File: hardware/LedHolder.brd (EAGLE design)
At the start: 8 x 8 mm, 5 parts

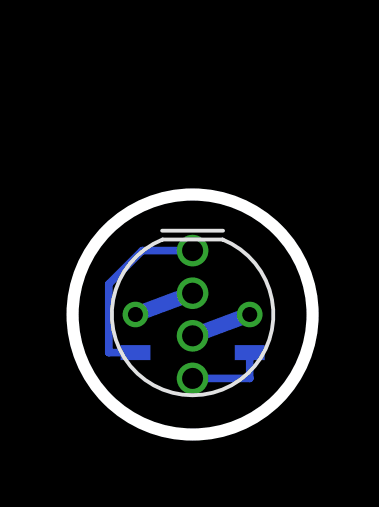
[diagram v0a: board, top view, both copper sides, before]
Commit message: More LedHolder updates
I switched the DataIn and DataOut connections to be through hole as
well since the holes hold the wire in place to make it easier for
soldering.
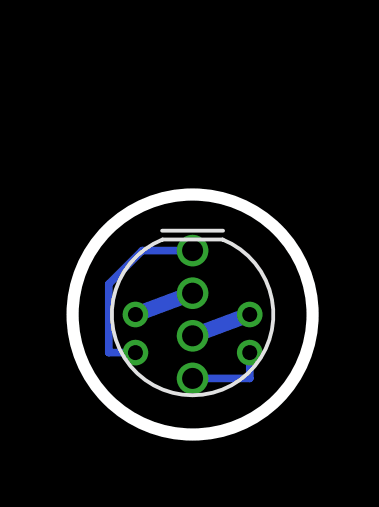
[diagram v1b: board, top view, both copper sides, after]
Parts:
- E$2, E$3: device adam_custom:PAD1MMX.5MM -> adam_custom:TP_5MM
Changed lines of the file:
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@@
 <element name="3" library="adam_custom" package="TP_5MM" value="" x="6.223" y="4.318"/>
 <element name="2" library="adam_custom" package="TP_5MM" value="" x="2.413" y="4.318"/>
-<element name="E$2" library="adam_custom" package="PAD1MMX.5MM" value="" x="6.223" y="3.048" rot="MR0"/>
-<element name="E$3" library="adam_custom" package="PAD1MMX.5MM" value="" x="2.413" y="3.048" rot="MR0"/>
+<element name="E$2" library="adam_custom" package="TP_5MM" value="" x="6.223" y="3.048" rot="MR0"/>
+<element name="E$3" library="adam_custom" package="TP_5MM" value="" x="2.413" y="3.048" rot="MR0"/>
 </elements>
 <signals>

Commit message: Create new LED holder PCB
The new PCB is rectangular and will extend horizontally from the end of
the branch wires. The LED will be bent at 90 degrees after being
soldered into this board so that it lays horizontally as well. I will
finalize the design once I have the flat cable in hand (currently on
order).
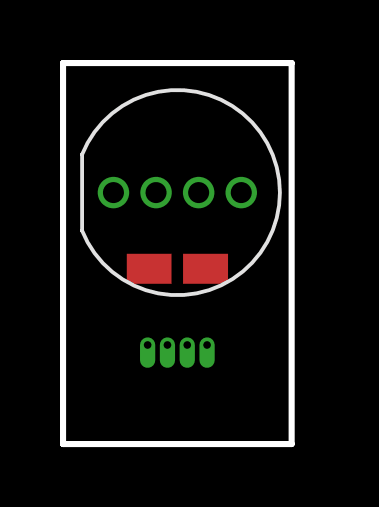
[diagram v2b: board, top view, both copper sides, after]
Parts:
- removed 2, 3: (no value), adam_custom:TP_5MM
- E$1: device adam_custom:LED-RGB-THRU -> adam_custom:NEOPIXEL_5MM_TH
- E$2: device adam_custom:TP_5MM -> adam_custom:NEOPIXEL_BRANCH_4WIRE
- E$3: value (none) -> 0.1uF; device adam_custom:TP_5MM -> adafruit:R0805W
- moved E$1 4.10 mm to (3.81, 8.38), turned to 180 degrees
- moved E$3 3.12 mm to (3.81, 5.84), flipped to the top
- moved E$2 2.43 mm to (3.81, 3.30), flipped to the top
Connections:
- net S$1: now also E$1.GROUND, E$2.P$1, E$3.1; no longer 2.P$1, E$1.2
- net S$2: now also E$1.5V, E$2.P$2, E$3.2; no longer 3.P$1, E$1.3
- net S$3: now also E$1.DATA_OUT, E$2.P$3; no longer E$1.1, E$3.P$1
- net S$4: now also E$1.DATA_IN, E$2.P$4; no longer E$1.4, E$2.P$1
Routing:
- net S$3: track 6.43 -> 0.00 mm
- net S$4: track 2.77 -> 0.00 mm
- net S$2: track 2.03 -> 0.00 mm
- net S$1: track 2.03 -> 0.00 mm
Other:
- board size 8 x 8 mm -> 7.6 x 12.7 mm
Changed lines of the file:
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@@
 <setting verticaltext="up"/>
 </settings>
-<grid distance="0.05" unitdist="inch" unit="inch" style="lines" multiple="1" display="yes" altdistance="0.01" altunitdist="inch" altunit="inch"/>
+<grid distance="0.05" unitdist="inch" unit="mil" style="lines" multiple="1" display="yes" altdistance="0.01" altunitdist="inch" altunit="mil"/>
 <layers>
 <layer number="1" name="Top" color="4" fill="1" visible="yes" active="yes"/>
@@
 <board>
 <plain>
-<circle x="4.318" y="4.318" radius="4" width="0.4064" layer="20"/>
-<text x="3.048" y="4.826" size="1.27" layer="22" font="vector" rot="MR0">-</text>
-<text x="6.604" y="4.826" size="1.27" layer="22" font="vector" rot="MR0">+</text>
-<text x="3.302" y="2.032" size="0.508" layer="22" font="vector" rot="MR0">Out</text>
-<text x="6.35" y="2.032" size="0.508" layer="22" font="vector" rot="MR0">In</text>
-<wire x1="3.302" y1="7.112" x2="5.334" y2="7.112" width="0.127" layer="21"/>
+<wire x1="0" y1="0" x2="0" y2="12.7" width="0.2032" layer="20"/>
+<wire x1="0" y1="12.7" x2="7.62" y2="12.7" width="0.2032" layer="20"/>
+<wire x1="7.62" y1="12.7" x2="7.62" y2="0" width="0.2032" layer="20"/>
+<wire x1="7.62" y1="0" x2="0" y2="0" width="0.2032" layer="20"/>
+<text x="5.588" y="0.508" size="1.016" layer="51" font="vector">In</text>
+<text x="0.508" y="0.508" size="1.016" layer="51" font="vector">Out</text>
+<text x="2.54" y="1.27" size="1.016" layer="51" font="vector">-</text>
+<text x="4.572" y="1.27" size="1.016" layer="51" font="vector">+</text>
 </plain>
 <attributes>
@@
 </class>
 </classes>
-<designrules name="LaenPCBOrder">
-<description language="de">&lt;b&gt;EAGLE Design Rules&lt;/b&gt;
+<designrules name="oshpark-2layer">
+<description language="en">&lt;b&gt;OSH Park Design Rules&lt;/b&gt;
 &lt;p&gt;
-Die Standard-Design-Rules sind so gewählt, dass sie für
-die meisten Anwendungen passen. Sollte ihre Platine
-besondere Anforderungen haben, treffen Sie die erforderlichen
-Einstellungen hier und speichern die Design Rules unter
-einem neuen Namen ab.</description>
-<description language="en">&lt;b&gt;Laen's PCB Order Design Rules&lt;/b&gt;
+Please make sure your boards conform to these design rules.
+&lt;/p&gt;
 &lt;p&gt;
-Please make sure your boards conform to these design rules.</description>
+Note, that not all DRC settings must be set by the manufacturer. Several can be adjusted for the design, including those listed on our docs page here.
+&lt;a href=&quot;http://docs.oshpark.com/design-tools/eagle/design-rules-files/&quot;&gt;Adjustable Settings&lt;/a&gt;
+&lt;/p&gt;</description>
 <param name="layerSetup" value="(1*16)"/>
-<param name="mtCopper" value="0.0356mm 0.0356mm 0.0356mm 0.0356mm 0.0356mm 0.0356mm 0.0356mm 0.0356mm 0.0356mm 0.0356mm 0.0356mm 0.0356mm 0.0356mm 0.0356mm 0.0356mm 0.0356mm"/>
-<param name="mtIsolate" value="1.5011mm 0.1499mm 0.2007mm 0.1499mm 0.2007mm 0.1499mm 0.2007mm 0.1499mm 0.2007mm 0.1499mm 0.2007mm 0.1499mm 0.2007mm 0.1499mm 0.2007mm"/>
+<param name="mtCopper" value="0.035559375mm 0.0356mm 0.0356mm 0.0356mm 0.0356mm 0.0356mm 0.0356mm 0.0356mm 0.0356mm 0.0356mm 0.0356mm 0.0356mm 0.0356mm 0.0356mm 0.0356mm 0.035559375mm"/>
+<param name="mtIsolate" value="1.6mm 0.1499mm 0.2007mm 0.1499mm 0.2007mm 0.1499mm 0.2007mm 0.1499mm 0.2007mm 0.1499mm 0.2007mm 0.1499mm 0.2007mm 0.1499mm 0.2007mm"/>
 <param name="mdWireWire" value="6mil"/>
 <param name="mdWirePad" value="6mil"/>
@@
 <param name="mdSmdStop" value="0mil"/>
 <param name="msWidth" value="6mil"/>
-<param name="msDrill" value="13mil"/>
-<param name="msMicroVia" value="13mil"/>
+<param name="msDrill" value="10mil"/>
+<param name="msMicroVia" value="10mil"/>
 <param name="msBlindViaRatio" value="0.5"/>
 <param name="rvPadTop" value="0.25"/>
@@
 <param name="rvMicroViaOuter" value="0.25"/>
 <param name="rvMicroViaInner" value="0.25"/>
-<param name="rlMinPadTop" value="7mil"/>
+<param name="rlMinPadTop" value="5mil"/>
 <param name="rlMaxPadTop" value="20mil"/>
-<param name="rlMinPadInner" value="7mil"/>
+<param name="rlMinPadInner" value="5mil"/>
 <param name="rlMaxPadInner" value="20mil"/>
-<param name="rlMinPadBottom" value="7mil"/>
+<param name="rlMinPadBottom" value="5mil"/>
 <param name="rlMaxPadBottom" value="20mil"/>
-<param name="rlMinViaOuter" value="7mil"/>
+<param name="rlMinViaOuter" value="5mil"/>
 <param name="rlMaxViaOuter" value="20mil"/>
-<param name="rlMinViaInner" value="7mil"/>
+<param name="rlMinViaInner" value="5mil"/>
 <param name="rlMaxViaInner" value="20mil"/>
-<param name="rlMinMicroViaOuter" value="4mil"/>
+<param name="rlMinMicroViaOuter" value="5mil"/>
 <param name="rlMaxMicroViaOuter" value="20mil"/>
-<param name="rlMinMicroViaInner" value="4mil"/>
+<param name="rlMinMicroViaInner" value="5mil"/>
 <param name="rlMaxMicroViaInner" value="20mil"/>
 <param name="psTop" value="-1"/>
@@
 <param name="mvStopFrame" value="1"/>
 <param name="mvCreamFrame" value="0"/>
-<param name="mlMinStopFrame" value="3mil"/>
-<param name="mlMaxStopFrame" value="3mil"/>
+<param name="mlMinStopFrame" value="2.5mil"/>
+<param name="mlMaxStopFrame" value="2.5mil"/>
 <param name="mlMinCreamFrame" value="0mil"/>
 <param name="mlMaxCreamFrame" value="0mil"/>
@@
 </autorouter>
 <elements>
-<element name="E$1" library="adam_custom" package="LED-RGB-THRU" value="" x="4.318" y="4.318" rot="R90"/>
-<element name="3" library="adam_custom" package="TP_5MM" value="" x="6.223" y="4.318"/>
-<element name="2" library="adam_custom" package="TP_5MM" value="" x="2.413" y="4.318"/>
-<element name="E$2" library="adam_custom" package="TP_5MM" value="" x="6.223" y="3.048" rot="MR0"/>
-<element name="E$3" library="adam_custom" package="TP_5MM" value="" x="2.413" y="3.048" rot="MR0"/>
+<element name="E$1" library="adam_custom" package="NEOPIXEL_5MM_TH" value="" x="3.81" y="8.382" rot="R180"/>
+<element name="E$2" library="adam_custom" package="NEOPIXEL_BRANCH_4WIRE" value="" x="3.81" y="3.302"/>
+<element name="E$3" library="adafruit" package="R0805W" value="0.1uF" x="3.81" y="5.842" smashed="yes">
+<attribute name="VALUE" x="2.413" y="3.937" size="0.8128" layer="27" font="vector"/>
+</element>
 </elements>
 <signals>
 <signal name="S$1">
-<contactref element="E$1" pad="2"/>
-<contactref element="2" pad="P$1"/>
-<wire x1="4.318" y1="5.028" x2="2.413" y2="4.318" width="0.508" layer="16"/>
+<contactref element="E$3" pad="1"/>
+<contactref element="E$1" pad="GROUND"/>
+<wire x1="3.1" y1="8.382" x2="2.87" y2="5.842" width="0" layer="19" extent="1-16"/>
+<contactref element="E$2" pad="P$1"/>
+<wire x1="2.87" y1="5.842" x2="3.4798" y2="3.302" width="0" layer="19" extent="1-16"/>
 </signal>
 <signal name="S$2">
-<contactref element="E$1" pad="3"/>
-<contactref element="3" pad="P$1"/>
-<wire x1="6.223" y1="4.318" x2="4.318" y2="3.608" width="0.508" layer="16"/>
+<contactref element="E$3" pad="2"/>
+<contactref element="E$1" pad="5V"/>
+<wire x1="4.52" y1="8.382" x2="4.75" y2="5.842" width="0" layer="19" extent="1-16"/>
+<contactref element="E$2" pad="P$2"/>
+<wire x1="4.75" y1="5.842" x2="4.1402" y2="3.302" width="0" layer="19" extent="1-16"/>
 </signal>
 <signal name="S$3">
-<contactref element="E$1" pad="1"/>
-<contactref element="E$3" pad="P$1"/>
-<wire x1="2.413" y1="3.048" x2="1.524" y2="3.048" width="0.254" layer="16"/>
-<wire x1="1.524" y1="3.048" x2="1.524" y2="5.334" width="0.254" layer="16"/>
-<wire x1="1.524" y1="5.334" x2="2.638" y2="6.448" width="0.254" layer="16"/>
-<wire x1="2.638" y1="6.448" x2="4.318" y2="6.448" width="0.254" layer="16"/>
+<contactref element="E$2" pad="P$3"/>
+<contactref element="E$1" pad="DATA_OUT"/>
+<wire x1="1.68" y1="8.382" x2="2.8194" y2="3.302" width="0" layer="19" extent="1-16"/>
 </signal>
 <signal name="S$4">
-<contactref element="E$1" pad="4"/>
-<contactref element="E$2" pad="P$1"/>
-<wire x1="6.223" y1="3.048" x2="6.223" y2="2.188" width="0.254" layer="16"/>
-<wire x1="6.223" y1="2.188" x2="4.318" y2="2.188" width="0.254" layer="16"/>
+<contactref element="E$2" pad="P$4"/>
+<contactref element="E$1" pad="DATA_IN"/>
+<wire x1="5.94" y1="8.382" x2="4.8006" y2="3.302" width="0" layer="19" extent="1-16"/>
 </signal>
 </signals>
